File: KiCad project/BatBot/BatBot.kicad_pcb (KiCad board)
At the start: 4 copper layers, 56 parts, among them J1 54550-1271, U1 STM32F439ZIYx, U2 nRF24L01P, U3 MPU-9250, U4 LM1117MPX-3_3_NOPB, X1 NX3225GD-8MHZ-STD-CRA-3, X2 XRCHA16M000F0A01R0

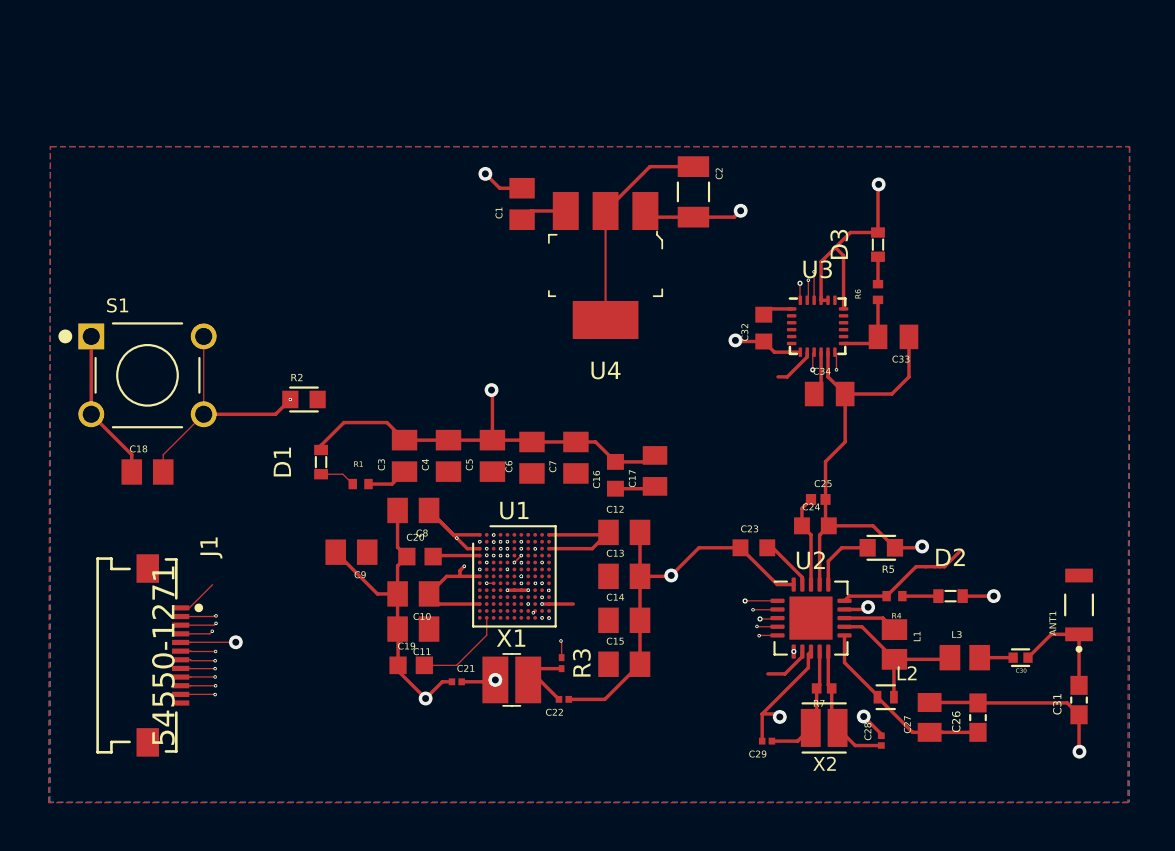
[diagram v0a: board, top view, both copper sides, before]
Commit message: fix PCBways errors
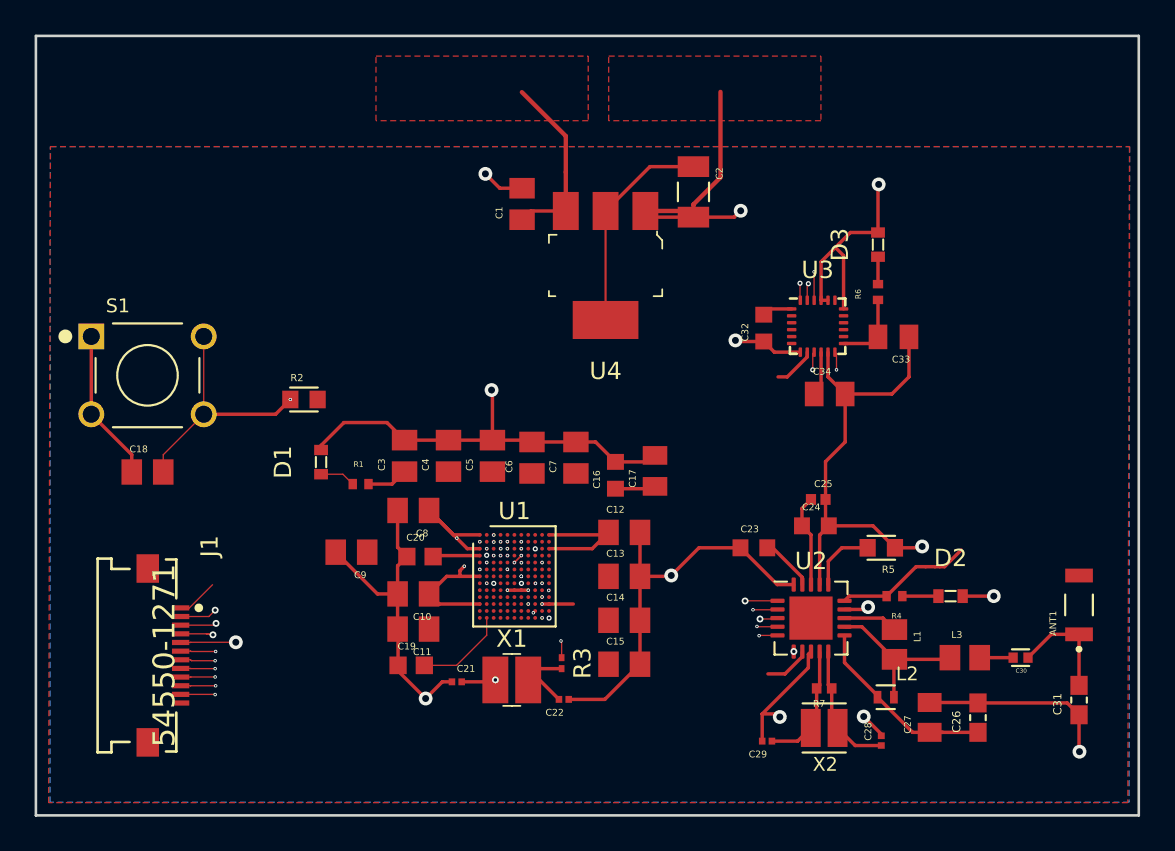
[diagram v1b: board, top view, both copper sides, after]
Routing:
- net GND: track 153.9 -> 163.6 mm, vias 22 -> 23
- net Net-(C1-Pad1): track 2.89 -> 10.8 mm
- added copper zone on F.Cu, net GND
- added copper zone on F.Cu, net Net-(C1-Pad1)
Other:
- board outline added: 63.8 x 45.1 mm

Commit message: 4/4mil spacing update
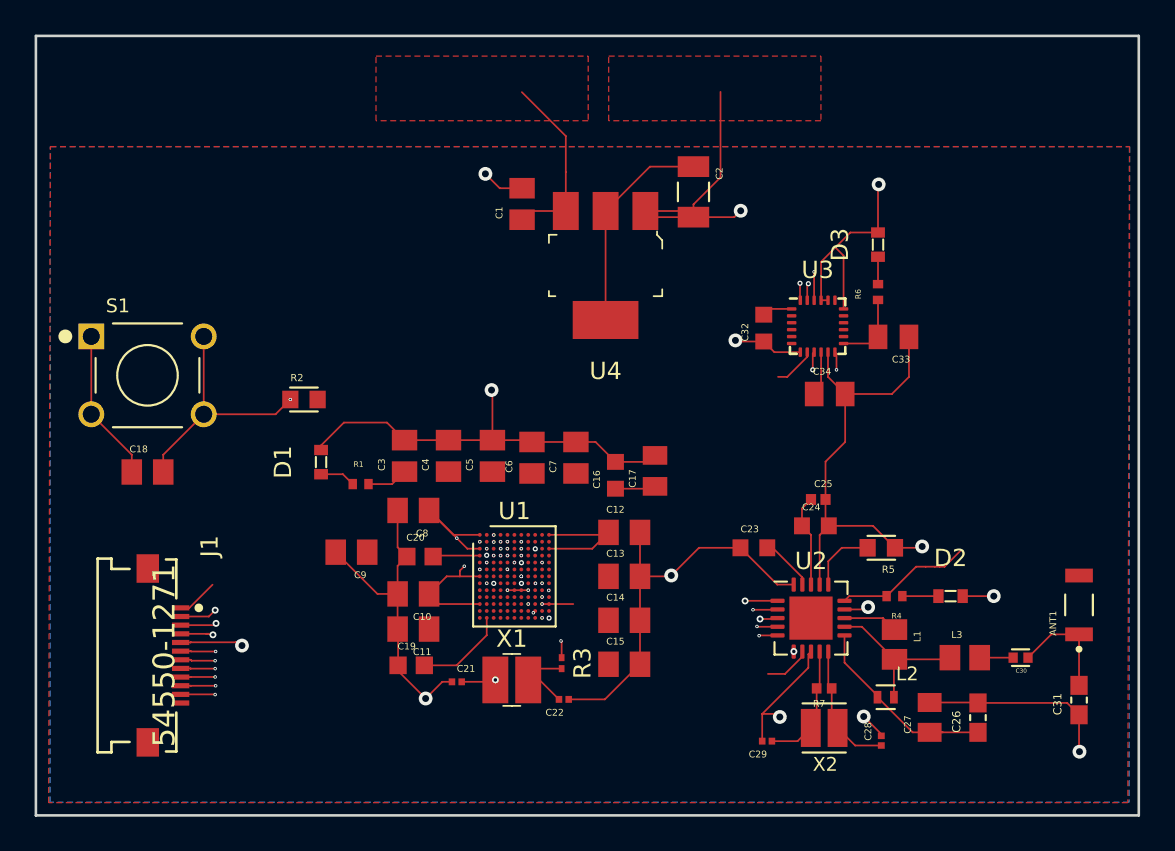
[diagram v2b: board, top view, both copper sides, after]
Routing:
- net SPI1-MOSI: track 41.6 -> 43.9 mm
- net USART1-RX: track 23.2 -> 22.8 mm, vias 2 -> 4
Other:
- net class Default: clearance 0.1 -> 0.1016; trace_width 0.0762 -> 0.1016
- rule trace_clearance: 0.1 -> 0.1016
- rule trace_min: 0.0762 -> 0.1016
